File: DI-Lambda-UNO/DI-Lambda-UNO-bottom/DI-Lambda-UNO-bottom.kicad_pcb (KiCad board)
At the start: 2 copper layers, 38.2 x 128.2 mm, 55 parts, among them J1 CONN_02X04, J10 CONN_02X04, J11 CONN_02X04, J13 CONN_02X04, J15 CONN_01X06, J16 CONN_01X06, J17 CONN_02X03, J18 USB_OTG, J2 Conn_01X01, J3 CONN_02X04, J4 Conn_01X01, J5 CONN_02X04, J6 CONN_02X04, J7 CONN_02X04, J8 CONN_02X04, J9 CONN_02X04, Q1 AO3400, SW1 RESET, U2 USBLC6-2SC6, U3 ATMEGA32U4-MU, U4 3.3v LDO, U5 AP3032, Y1 8Mhz

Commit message: DI-Lambda UNO bottom cleanup
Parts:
- removed svg2mod: G***, svg2mod:logo1-for-Kicad-mask
- removed svg2mod: G***, svg2mod:logo1-for-Kicad-cu
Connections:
- net /SS renamed Net-(U3-Pad8)

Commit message: Fix spring contact module name
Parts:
- J15, J16: footprint Sprint-contact-connector-2:Spring-contact-connector-2.5x6 -> Spring-contact-connector-2:Spring-contact-connector-2.5x6
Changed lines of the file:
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@@
     )
   )
-  (module Sprint-contact-connector-2:Spring-contact-connector-2.5x6 (layer F.Cu)
+  (module Spring-contact-connector-2:Spring-contact-connector-2.5x6 (layer F.Cu)
     (at 150.355 51.57 180)
     (fp_text reference J16 (at 8 -3.9) (layer F.SilkS)
@@
     (pad ~ smd rect (at 8.75 0.333 180) (size 2 2) (layers F.Cu F.Paste F.Mask))
   )
-  (module Sprint-contact-connector-2:Spring-contact-connector-2.5x6 (layer F.Cu)
+  (module Spring-contact-connector-2:Spring-contact-connector-2.5x6 (layer F.Cu)
     (at 150.355 153.57)
     (fp_text reference J15 (at -10.5 -0.25 90) (layer F.SilkS)

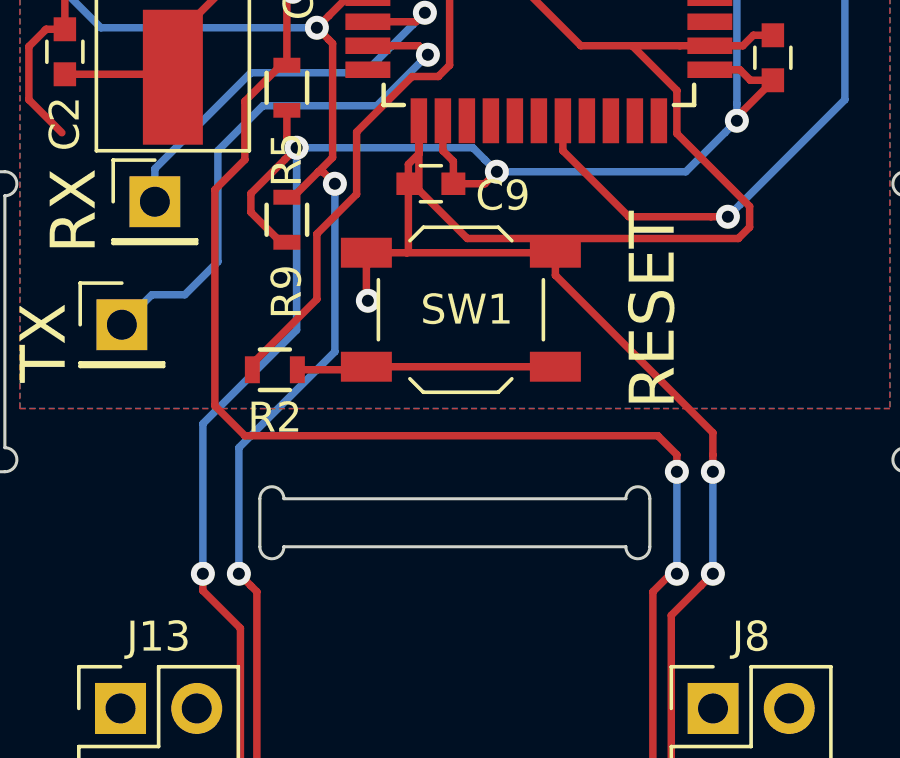
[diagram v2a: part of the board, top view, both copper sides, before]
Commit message: Swap SDA/SCL on the main board
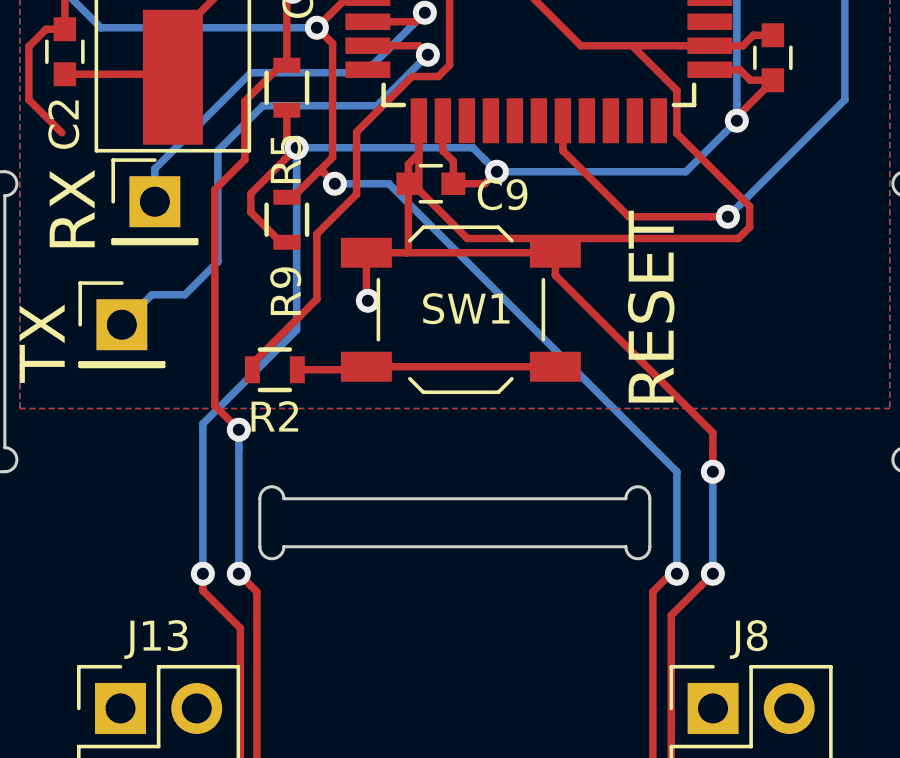
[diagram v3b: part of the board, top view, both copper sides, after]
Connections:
- J15 pad 2: /SCL -> /SDA
- J15 pad 3: /SDA -> /SCL
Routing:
- net /SCL: track 136.0 -> 123.8 mm
- net /SDA: track 123.3 -> 126.1 mm
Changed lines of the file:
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@@
-(kicad_pcb (version 20170123) (host pcbnew "(2017-07-27 revision 3ee2f80)-test1")
+(kicad_pcb (version 20170123) (host pcbnew "(2017-09-07 revision 3b08636)-master")
   (general
     (thickness 1.6)
     (drawings 105)
-    (tracks 626)
+    (tracks 625)
     (zones 0)
     (modules 53)
@@
     (aux_axis_origin 131.255 35.97)
     (grid_origin 131.255 164.17)
-    (visible_elements FFFFFF7F)
+    (visible_elements FFFFEF7F)
     (pcbplotparams
       (layerselection 0x000f0_ffffffff)
       (usegerberextensions true)
+      (usegerberattributes true)
+      (usegerberadvancedattributes true)
+      (creategerberjobfile true)
       (excludeedgelayer false)
       (linewidth 0.100000)
@@
       (net 93 /VCC))
     (pad 3 smd rect (at 1.25 -2.5) (size 1 1) (layers F.Cu F.Paste F.Mask)
-      (net 96 /SDA))
-    (pad 2 smd rect (at 3.75 -2.5) (size 1 1) (layers F.Cu F.Paste F.Mask)
       (net 104 /SCL))
+    (pad 2 smd rect (at 3.75 -2.5) (size 1 1) (layers F.Cu F.Paste F.Mask)
+      (net 96 /SDA))
     (pad 1 smd rect (at 6.25 -2.5) (size 1 1) (layers F.Cu F.Paste F.Mask)
       (net 86 GND))
@@
   (via (at 146.755 81.47) (size 0.8) (drill 0.4) (layers F.Cu B.Cu) (net 95))
   (segment (start 148.855282 81.47) (end 146.755 81.47) (width 0.25) (layer F.Cu) (net 95))
+  (segment (start 146.355 97.07) (end 148.155 97.07) (width 0.25) (layer B.Cu) (net 96))
+  (segment (start 148.155 97.07) (end 157.755 106.67) (width 0.25) (layer B.Cu) (net 96))
+  (segment (start 157.755 106.67) (end 157.755 110.07) (width 0.25) (layer B.Cu) (net 96))
+  (segment (start 142.355 104.47) (end 143.155 105.27) (width 0.25) (layer F.Cu) (net 104))
+  (via (at 143.155 105.27) (size 0.8) (drill 0.4) (layers F.Cu B.Cu) (net 104))
+  (segment (start 143.155 105.27) (end 143.355 105.47) (width 0.25) (layer F.Cu) (net 104))
+  (segment (start 143.155 105.87) (end 143.155 105.27) (width 0.25) (layer B.Cu) (net 104))
+  (segment (start 151.605 151.07) (end 151.605 138.32) (width 0.25) (layer F.Cu) (net 104))
+  (segment (start 143.754999 126.270001) (end 143.754999 110.669999) (width 0.25) (layer F.Cu) (net 104))
+  (segment (start 143.355 126.67) (end 143.754999 126.270001) (width 0.25) (layer F.Cu) (net 104))
+  (segment (start 143.754999 110.669999) (end 143.554999 110.469999) (width 0.25) (layer F.Cu) (net 104))
+  (segment (start 143.554999 110.469999) (end 143.155 110.07) (width 0.25) (layer F.Cu) (net 104))
   (segment (start 144.555001 55.869999) (end 144.955 55.47) (width 0.25) (layer B.Cu) (net 96))
   (segment (start 145.755 91.87001) (end 138.55501 91.87001) (width 0.25) (layer B.Cu) (net 96))
@@
   (segment (start 138.55501 91.87001) (end 134.555 87.87) (width 0.25) (layer B.Cu) (net 96))
   (segment (start 143.104989 57.320011) (end 144.555001 55.869999) (width 0.25) (layer B.Cu) (net 96))
-  (segment (start 146.355 97.07) (end 146.355 102.67) (width 0.25) (layer B.Cu) (net 96))
-  (segment (start 146.355 102.67) (end 143.155 105.87) (width 0.25) (layer B.Cu) (net 96))
-  (segment (start 143.155 105.87) (end 143.155 110.07) (width 0.25) (layer B.Cu) (net 96))
-  (segment (start 143.754999 126.270001) (end 143.754999 110.669999) (width 0.25) (layer F.Cu) (net 96))
-  (segment (start 143.754999 110.669999) (end 143.554999 110.469999) (width 0.25) (layer F.Cu) (net 96))
-  (segment (start 143.355 126.67) (end 143.754999 126.270001) (width 0.25) (layer F.Cu) (net 96))
-  (segment (start 143.554999 110.469999) (end 143.155 110.07) (width 0.25) (layer F.Cu) (net 96))
-  (via (at 143.155 110.07) (size 0.8) (drill 0.4) (layers F.Cu B.Cu) (net 96))
-  (segment (start 143.355 130.07) (end 143.355 126.67) (width 0.25) (layer B.Cu) (net 96))
-  (via (at 143.355 126.67) (size 0.8) (drill 0.4) (layers F.Cu B.Cu) (net 96))
-  (segment (start 143.754999 130.469999) (end 143.355 130.07) (width 0.25) (layer F.Cu) (net 96))
-  (segment (start 151.605 138.32) (end 143.754999 130.469999) (width 0.25) (layer F.Cu) (net 96))
-  (segment (start 151.605 151.07) (end 151.605 138.32) (width 0.25) (layer F.Cu) (net 96))
-  (via (at 143.355 130.07) (size 0.8) (drill 0.4) (layers F.Cu B.Cu) (net 96))
+  (segment (start 143.155 105.87) (end 143.155 110.07) (width 0.25) (layer B.Cu) (net 104))
+  (via (at 143.155 110.07) (size 0.8) (drill 0.4) (layers F.Cu B.Cu) (net 104))
+  (segment (start 143.355 130.07) (end 143.355 126.67) (width 0.25) (layer B.Cu) (net 104))
+  (via (at 143.355 126.67) (size 0.8) (drill 0.4) (layers F.Cu B.Cu) (net 104))
+  (segment (start 143.754999 130.469999) (end 143.355 130.07) (width 0.25) (layer F.Cu) (net 104))
+  (segment (start 151.605 138.32) (end 143.754999 130.469999) (width 0.25) (layer F.Cu) (net 104))
+  (via (at 143.355 130.07) (size 0.8) (drill 0.4) (layers F.Cu B.Cu) (net 104))
   (segment (start 145.805 96.67) (end 146.280002 96.194998) (width 0.25) (layer F.Cu) (net 96))
   (segment (start 144.955 97.52) (end 145.805 96.67) (width 0.25) (layer F.Cu) (net 96))
@@
   (segment (start 151.555 45.27) (end 151.305 45.02) (width 0.25) (layer F.Cu) (net 103))
   (segment (start 151.305 45.02) (end 151.305 44.27) (width 0.25) (layer F.Cu) (net 103))
+  (segment (start 154.105 151.07) (end 154.105 133.52) (width 0.25) (layer F.Cu) (net 96))
+  (segment (start 154.105 133.52) (end 157.155001 130.469999) (width 0.25) (layer F.Cu) (net 96))
+  (segment (start 157.155001 130.469999) (end 157.555 130.07) (width 0.25) (layer F.Cu) (net 96))
+  (segment (start 157.555 126.67001) (end 156.955 126.07001) (width 0.25) (layer F.Cu) (net 96))
+  (segment (start 157.555 110.07) (end 157.755 110.07) (width 0.25) (layer F.Cu) (net 96))
+  (segment (start 156.955 110.67) (end 157.555 110.07) (width 0.25) (layer F.Cu) (net 96))
+  (via (at 157.755 110.07) (size 0.8) (drill 0.4) (layers F.Cu B.Cu) (net 96))
+  (segment (start 156.955 126.07001) (end 156.955 110.67) (width 0.25) (layer F.Cu) (net 96))
+  (segment (start 142.355 97.27) (end 142.355 104.47) (width 0.25) (layer F.Cu) (net 104))
+  (segment (start 144.555 93.12) (end 143.355 94.32) (width 0.25) (layer F.Cu) (net 104))
+  (segment (start 143.355 94.32) (end 143.355 96.27) (width 0.25) (layer F.Cu) (net 104))
+  (segment (start 143.355 96.27) (end 142.355 97.27) (width 0.25) (layer F.Cu) (net 104))
   (segment (start 144.955 90.67) (end 138.555 90.67) (width 0.25) (layer B.Cu) (net 104))
   (segment (start 138.555 90.67) (end 135.155 87.27) (width 0.25) (layer B.Cu) (net 104))
@@
   (segment (start 148.655 57.17) (end 149.755 56.07) (width 0.25) (layer B.Cu) (net 104))
   (segment (start 144.755 93.12) (end 144.555 93.12) (width 0.25) (layer F.Cu) (net 104))
-  (segment (start 144.555 93.12) (end 143.355 94.32) (width 0.25) (layer F.Cu) (net 104))
-  (segment (start 143.355 94.32) (end 143.355 96.27) (width 0.25) (layer F.Cu) (net 104))
-  (segment (start 143.355 96.27) (end 142.355 97.27) (width 0.25) (layer F.Cu) (net 104))
-  (segment (start 157.120685 105.47) (end 157.755 106.104315) (width 0.25) (layer F.Cu) (net 104))
-  (segment (start 142.355 97.27) (end 142.355 104.47) (width 0.25) (layer F.Cu) (net 104))
-  (segment (start 142.355 104.47) (end 143.355 105.47) (width 0.25) (layer F.Cu) (net 104))
-  (segment (start 143.355 105.47) (end 157.120685 105.47) (width 0.25) (layer F.Cu) (net 104))
-  (segment (start 157.755 106.104315) (end 157.755 106.67) (width 0.25) (layer F.Cu) (net 104))
-  (segment (start 157.755 110.07) (end 157.755 106.67) (width 0.25) (layer B.Cu) (net 104))
-  (via (at 157.755 106.67) (size 0.8) (drill 0.4) (layers F.Cu B.Cu) (net 104))
-  (segment (start 157.555 110.07) (end 157.755 110.07) (width 0.25) (layer F.Cu) (net 104))
-  (segment (start 156.955 110.67) (end 157.555 110.07) (width 0.25) (layer F.Cu) (net 104))
-  (via (at 157.755 110.07) (size 0.8) (drill 0.4) (layers F.Cu B.Cu) (net 104))
-  (segment (start 156.955 126.07001) (end 156.955 110.67) (width 0.25) (layer F.Cu) (net 104))
-  (segment (start 157.555 126.67001) (end 156.955 126.07001) (width 0.25) (layer F.Cu) (net 104))
-  (via (at 157.555 126.67001) (size 0.8) (drill 0.4) (layers F.Cu B.Cu) (net 104))
-  (segment (start 157.555 130.07) (end 157.555 126.67001) (width 0.25) (layer B.Cu) (net 104))
-  (segment (start 157.155001 130.469999) (end 157.555 130.07) (width 0.25) (layer F.Cu) (net 104))
-  (segment (start 154.105 133.52) (end 157.155001 130.469999) (width 0.25) (layer F.Cu) (net 104))
-  (segment (start 154.105 151.07) (end 154.105 133.52) (width 0.25) (layer F.Cu) (net 104))
-  (via (at 157.555 130.07) (size 0.8) (drill 0.4) (layers F.Cu B.Cu) (net 104))
+  (via (at 157.555 126.67001) (size 0.8) (drill 0.4) (layers F.Cu B.Cu) (net 96))
+  (segment (start 157.555 130.07) (end 157.555 126.67001) (width 0.25) (layer B.Cu) (net 96))
+  (via (at 157.555 130.07) (size 0.8) (drill 0.4) (layers F.Cu B.Cu) (net 96))
   (segment (start 144.755 90.87) (end 144.955 90.67) (width 0.25) (layer F.Cu) (net 104))
   (segment (start 145.354999 90.270001) (end 144.955 90.67) (width 0.25) (layer F.Cu) (net 104))

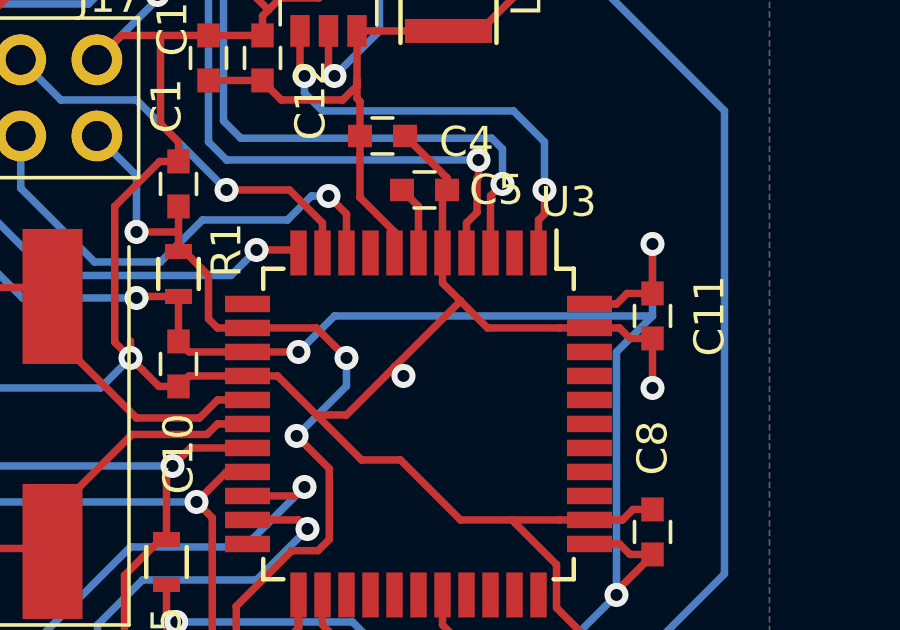
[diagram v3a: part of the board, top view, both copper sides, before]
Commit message: Connect UCAP to VCC on the main board
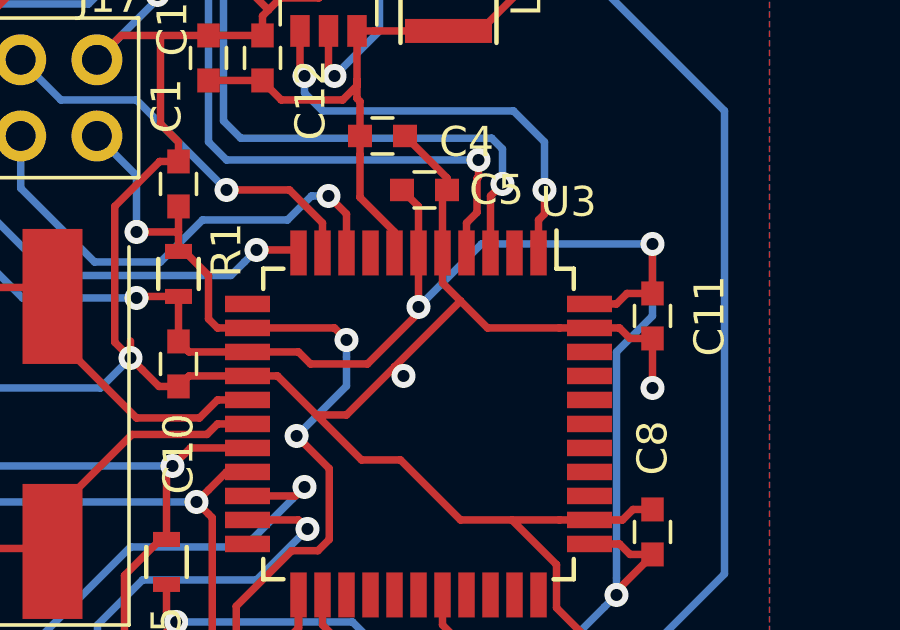
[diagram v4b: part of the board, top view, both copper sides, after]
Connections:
- C5 pad 1: Net-(C5-Pad1) -> /VCC
- U3 pad 6: Net-(C5-Pad1) -> /VCC
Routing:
- net /VCC: track 173.8 -> 179.4 mm
- net Net-(C5-Pad1): track 2.33 -> 0.00 mm
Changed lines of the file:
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@@
     (thickness 1.6)
     (drawings 105)
-    (tracks 625)
+    (tracks 628)
     (zones 0)
     (modules 53)
-    (nets 132)
+    (nets 131)
   )
   (page A4)
@@
   (net 125 "Net-(C3-Pad1)")
   (net 126 "Net-(U3-Pad12)")
-  (net 127 "Net-(C5-Pad1)")
-  (net 128 "Net-(U3-Pad2)")
-  (net 129 "Net-(J18-Pad4)")
-  (net 130 "Net-(U3-Pad41)")
-  (net 131 "Net-(U3-Pad8)")
+  (net 127 "Net-(U3-Pad2)")
+  (net 128 "Net-(J18-Pad4)")
+  (net 129 "Net-(U3-Pad41)")
+  (net 130 "Net-(U3-Pad8)")
   (net_class Default "This is the default net class."
     (clearance 0.2)
@@
     (add_net "Net-(C2-Pad1)")
     (add_net "Net-(C3-Pad1)")
-    (add_net "Net-(C5-Pad1)")
     (add_net "Net-(F1-Pad2)")
     (add_net "Net-(J1-Pad1)")
@@
       (net 86 GND))
     (pad 1 smd rect (at -0.75 0) (size 0.8 0.75) (layers F.Cu F.Paste F.Mask)
-      (net 127 "Net-(C5-Pad1)"))
+      (net 93 /VCC))
     (model Capacitors_SMD.3dshapes/C_0603.wrl
       (at (xyz 0 0 0))
@@
       (net 103 "Net-(J18-Pad5)"))
     (pad 4 smd rect (at 2.8 0.8 270) (size 2.3 0.5) (layers F.Cu F.Paste F.Mask)
-      (net 129 "Net-(J18-Pad4)"))
+      (net 128 "Net-(J18-Pad4)"))
     (pad 3 smd rect (at 2.8 0 270) (size 2.3 0.5) (layers F.Cu F.Paste F.Mask)
       (net 97 "Net-(J18-Pad3)"))
@@
       (net 89 /BOOST_CTRL))
     (pad 2 smd rect (at -5.7 -3.2 270) (size 1.5 0.55) (layers F.Cu F.Paste F.Mask)
-      (net 128 "Net-(U3-Pad2)"))
+      (net 127 "Net-(U3-Pad2)"))
     (pad 3 smd rect (at -5.7 -2.4 270) (size 1.5 0.55) (layers F.Cu F.Paste F.Mask)
       (net 85 "Net-(R10-Pad1)"))
@@
       (net 86 GND))
     (pad 6 smd rect (at -5.7 0 270) (size 1.5 0.55) (layers F.Cu F.Paste F.Mask)
-      (net 127 "Net-(C5-Pad1)"))
+      (net 93 /VCC))
     (pad 7 smd rect (at -5.7 0.8 270) (size 1.5 0.55) (layers F.Cu F.Paste F.Mask)
       (net 83 /VBUS))
     (pad 8 smd rect (at -5.7 1.6 270) (size 1.5 0.55) (layers F.Cu F.Paste F.Mask)
-      (net 131 "Net-(U3-Pad8)"))
+      (net 130 "Net-(U3-Pad8)"))
     (pad 9 smd rect (at -5.7 2.4 270) (size 1.5 0.55) (layers F.Cu F.Paste F.Mask)
       (net 94 /SCK))
@@
       (net 108 "Net-(U3-Pad40)"))
     (pad 41 smd rect (at -1.6 -5.7) (size 1.5 0.55) (layers F.Cu F.Paste F.Mask)
-      (net 130 "Net-(U3-Pad41)"))
+      (net 129 "Net-(U3-Pad41)"))
     (pad 42 smd rect (at -2.4 -5.7) (size 1.5 0.55) (layers F.Cu F.Paste F.Mask)
       (net 107 "Net-(U3-Pad42)"))
@@
   (segment (start 153.405 60.87) (end 153.405 59.27) (width 0.25) (layer F.Cu) (net 92))
   (segment (start 153.405 59.27) (end 153.205 59.07) (width 0.25) (layer F.Cu) (net 92))
+  (segment (start 160.955 83.27) (end 155.255282 83.27) (width 0.25) (layer B.Cu) (net 93))
+  (segment (start 155.255282 83.27) (end 153.155282 85.37) (width 0.25) (layer B.Cu) (net 93))
+  (via (at 153.155282 85.37) (size 0.8) (drill 0.4) (layers F.Cu B.Cu) (net 93))
+  (segment (start 147.455282 86.87) (end 149.155 86.87) (width 0.25) (layer F.Cu) (net 93))
+  (segment (start 149.554999 87.269999) (end 151.455001 87.269999) (width 0.25) (layer F.Cu) (net 93))
+  (segment (start 151.455001 87.269999) (end 153.155282 85.569718) (width 0.25) (layer F.Cu) (net 93))
+  (segment (start 149.155 86.87) (end 149.554999 87.269999) (width 0.25) (layer F.Cu) (net 93))
+  (segment (start 153.155282 85.569718) (end 153.155282 83.57) (width 0.25) (layer F.Cu) (net 93))
   (segment (start 150.055 63.67) (end 150.455 63.27) (width 0.25) (layer B.Cu) (net 93))
   (segment (start 149.655 67.47) (end 149.655 65.27) (width 0.25) (layer B.Cu) (net 93))
@@
   (segment (start 143.555 97.395026) (end 144.680011 96.270015) (width 0.25) (layer F.Cu) (net 93))
   (segment (start 160.955 85.67) (end 160.955 83.27) (width 0.25) (layer B.Cu) (net 93))
-  (segment (start 150.355 85.67) (end 160.955 85.67) (width 0.25) (layer B.Cu) (net 93))
-  (segment (start 149.155 86.87) (end 150.355 85.67) (width 0.25) (layer B.Cu) (net 93))
-  (segment (start 147.455282 86.87) (end 149.155 86.87) (width 0.25) (layer F.Cu) (net 93))
-  (via (at 149.155 86.87) (size 0.8) (drill 0.4) (layers F.Cu B.Cu) (net 93))
   (segment (start 160.955 84.92) (end 160.955 83.27) (width 0.25) (layer F.Cu) (net 93))
   (via (at 160.955 83.27) (size 0.8) (drill 0.4) (layers F.Cu B.Cu) (net 93))
@@
   (segment (start 149.105 55.42) (end 149.755 56.07) (width 0.25) (layer F.Cu) (net 104))
   (via (at 149.755 56.07) (size 0.8) (drill 0.4) (layers F.Cu B.Cu) (net 104))
+  (segment (start 150.355001 86.070001) (end 150.755 86.47) (width 0.25) (layer F.Cu) (net 105))
+  (segment (start 147.455282 86.07) (end 150.355001 86.070001) (width 0.25) (layer F.Cu) (net 105))
+  (segment (start 150.755 87.035685) (end 150.755 86.47) (width 0.25) (layer B.Cu) (net 105))
+  (segment (start 149.091392 89.67) (end 150.755 88.006392) (width 0.25) (layer B.Cu) (net 105))
+  (via (at 150.755 86.47) (size 0.8) (drill 0.4) (layers F.Cu B.Cu) (net 105))
+  (segment (start 150.755 88.006392) (end 150.755 87.035685) (width 0.25) (layer B.Cu) (net 105))
   (segment (start 149.091392 89.67) (end 150.180001 90.758609) (width 0.25) (layer F.Cu) (net 105))
   (segment (start 150.180001 90.758609) (end 150.180001 93.118001) (width 0.25) (layer F.Cu) (net 105))
@@
   (segment (start 145.755 98.743004) (end 145.755 100.92) (width 0.25) (layer F.Cu) (net 105))
   (segment (start 143.605 103.07) (end 143.605 103.27) (width 0.25) (layer F.Cu) (net 105))
-  (segment (start 149.091392 89.67) (end 150.755 88.006392) (width 0.25) (layer B.Cu) (net 105))
   (via (at 149.091392 89.67) (size 0.8) (drill 0.4) (layers F.Cu B.Cu) (net 105))
-  (segment (start 150.755 88.006392) (end 150.755 87.635685) (width 0.25) (layer B.Cu) (net 105))
-  (segment (start 150.755 87.635685) (end 150.755 87.07) (width 0.25) (layer B.Cu) (net 105))
-  (segment (start 150.355001 86.670001) (end 150.755 87.07) (width 0.25) (layer F.Cu) (net 105))
-  (segment (start 147.455282 86.07) (end 149.755 86.07) (width 0.25) (layer F.Cu) (net 105))
-  (segment (start 149.755 86.07) (end 150.355001 86.670001) (width 0.25) (layer F.Cu) (net 105))
-  (via (at 150.755 87.07) (size 0.8) (drill 0.4) (layers F.Cu B.Cu) (net 105))
   (segment (start 143.755 82.87) (end 143.755 80.99) (width 0.25) (layer B.Cu) (net 105))
   (segment (start 143.755 80.99) (end 142.435 79.67) (width 0.25) (layer B.Cu) (net 105))
@@
   (segment (start 147.455282 88.47) (end 146.455282 88.47) (width 0.25) (layer F.Cu) (net 125))
   (segment (start 146.455282 88.47) (end 145.855282 89.07) (width 0.25) (layer F.Cu) (net 125))
-  (segment (start 153.155282 83.57) (end 153.155282 82.020282) (width 0.25) (layer F.Cu) (net 127))
-  (segment (start 153.155282 82.020282) (end 152.605 81.47) (width 0.25) (layer F.Cu) (net 127))
+  (segment (start 153.155282 83.57) (end 153.155282 82.020282) (width 0.25) (layer F.Cu) (net 93))
+  (segment (start 153.155282 82.020282) (end 152.605 81.47) (width 0.25) (layer F.Cu) (net 93))
   (zone (net 0) (net_name "") (layer F.Cu) (hatch edge 0.508)
     (connect_pads (clearance 0.508))
